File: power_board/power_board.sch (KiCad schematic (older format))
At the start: 84 parts, among them J1 PROG, J10 M4, J11 5V_1, J12 M5, J13 M6, J14 M7, J15 FAN, J16 Screw_Terminal_01x02, J17 MB_interface, J18 Conn_01x02_Female, J19 12V_1, J2 M1, J20 12V_2, J21 12V_3, J22 12V_4, J23 48V_1, J24 48V_2, J25 48V_3, J26 48V_4, J27 Screw_Terminal_01x02, J3 M2, J4 Conn_01x02_Female, J5 Conn_01x02_Female, J6 Conn_01x01_Male, J7 Conn_01x01_Male, J8 Screw_Terminal_01x02, J9 M3, SW1 SW_Push, U1 ACS758xCB-050B-PFF, U10 MAX31855KASA, U2 ACS758xCB-050B-PFF, U3 MCP2515-EST, U4 MAX31855KASA, U5 ATA6560,1, U6 BTS50085-1TMA, U7 ATmega328P-AU, U8 BTS50085-1TMA, U9 LM2596S-5, Y1 20Mhz, Y2 16Mhz

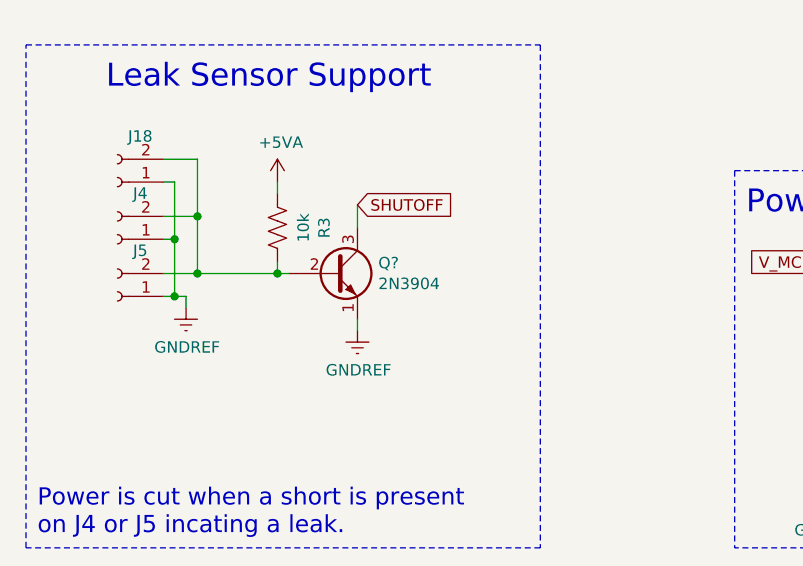
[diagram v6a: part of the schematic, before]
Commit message: selected new footprint for BJT for power shutoff
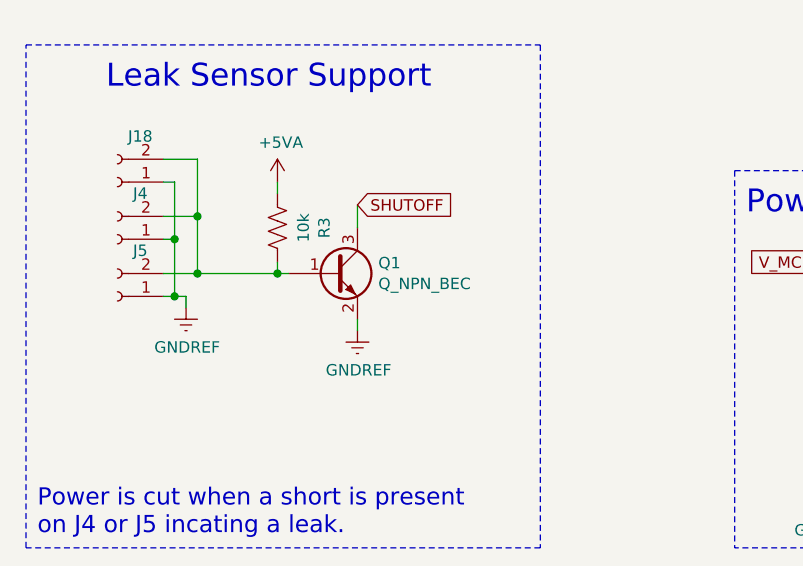
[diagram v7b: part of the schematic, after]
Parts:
- removed Q?: 2N3904, Package_TO_SOT_THT:TO-92_Inline, symbol Transistor_BJT:2N3904
- added Q1: Q_NPN_BEC, Package_TO_SOT_SMD:SOT-23, symbol Device:Q_NPN_BEC
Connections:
- net GNDREF: now also Q1.2 (E)
- net SHUTOFF: now also Q1.3 (C)
- net at J18.2 (Pin_2), J4.2 (Pin_2), J5.2 (Pin_2)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: now also Q1.1 (B)
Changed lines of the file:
@@
-$EndComp
-$Comp
-L power:+5V #PWR0139
-U 1 1 5BB11F6E
-P 6750 3550
-F 0 "#PWR0139" H 6750 3400 50  0001 C CNN
-F 1 "+5V" H 6765 3723 50  0000 C CNN
-F 2 "" H 6750 3550 50  0001 C CNN
-F 3 "" H 6750 3550 50  0001 C CNN
-	1    6750 3550
-	1    0    0    -1
 $EndComp
 $Comp
@@
 	7550 4300 7700 4300
 Connection ~ 7550 4300
-$Comp
-L power:+5V #PWR0142
-U 1 1 5BB53379
-P 7550 3950
-F 0 "#PWR0142" H 7550 3800 50  0001 C CNN
-F 1 "+5V" H 7565 4123 50  0000 C CNN
-F 2 "" H 7550 3950 50  0001 C CNN
-F 3 "" H 7550 3950 50  0001 C CNN
-	1    7550 3950
-	1    0    0    -1
-$EndComp
-Wire Wire Line
-	7550 4000 7550 3950
 $Comp
 L Connector:Screw_Terminal_01x02 J8
@@
 $EndComp
 $Comp
-L power:+5V #PWR0163
-U 1 1 5C02E9E2
-P 6750 5300
-F 0 "#PWR0163" H 6750 5150 50  0001 C CNN
-F 1 "+5V" H 6765 5473 50  0000 C CNN
-F 2 "" H 6750 5300 50  0001 C CNN
-F 3 "" H 6750 5300 50  0001 C CNN
-	1    6750 5300
-	1    0    0    -1
-$EndComp
-$Comp
 L power:GNDREF #PWR0164
 U 1 1 5C02E9E8
@@
 Connection ~ 7550 6050
 $Comp
-L power:+5V #PWR0166
-U 1 1 5C02EA0C
-P 7550 5700
-F 0 "#PWR0166" H 7550 5550 50  0001 C CNN
-F 1 "+5V" H 7565 5873 50  0000 C CNN
-F 2 "" H 7550 5700 50  0001 C CNN
-F 3 "" H 7550 5700 50  0001 C CNN
-	1    7550 5700
-	1    0    0    -1
-$EndComp
-Wire Wire Line
-	7550 5750 7550 5700
-$Comp
 L Connector:Screw_Terminal_01x02 J27
 U 1 1 5C02EA13
@@
 Text Notes 14850 7800 0    75   ~ 0
 ICSP Connections\n
-$Comp
-L Transistor_BJT:2N3904 Q?
-U 1 1 5BF7B85C
+Wire Wire Line
+	2150 8200 2150 8250
+Wire Wire Line
+	2500 8400 2500 8300
+Wire Wire Line
+	2500 8800 2500 8850
+Wire Wire Line
+	1800 8600 2150 8600
+$Comp
+L Device:Q_NPN_BEC Q1
+U 1 1 5C017B6E
 P 2400 8600
-F 0 "Q?" H 2591 8646 50  0000 L CNN
-F 1 "2N3904" H 2591 8555 50  0000 L CNN
-F 2 "Package_TO_SOT_THT:TO-92_Inline" H 2600 8525 50  0001 L CIN
-F 3 "https://www.fairchildsemi.com/datasheets/2N/2N3904.pdf" H 2400 8600 50  0001 L CNN
+F 0 "Q1" H 2591 8646 50  0000 L CNN
+F 1 "Q_NPN_BEC" H 2591 8555 50  0000 L CNN
+F 2 "Package_TO_SOT_SMD:SOT-23" H 2600 8700 50  0001 C CNN
+F 3 "~" H 2400 8600 50  0001 C CNN
 	1    2400 8600
 	1    0    0    -1
 $EndComp
 Wire Wire Line
-	2150 8200 2150 8250
-Wire Wire Line
-	2500 8400 2500 8300
-Wire Wire Line
-	2500 8800 2500 8850
-Wire Wire Line
-	1800 8600 2150 8600
+	7550 5750 7550 5700
+Wire Wire Line
+	7550 4000 7550 3950
+$Comp
+L power:+5V #PWR0142
+U 1 1 5BB53379
+P 7550 3950
+F 0 "#PWR0142" H 7550 3800 50  0001 C CNN
+F 1 "+5V" H 7565 4123 50  0000 C CNN
+F 2 "" H 7550 3950 50  0001 C CNN
+F 3 "" H 7550 3950 50  0001 C CNN
+	1    7550 3950
+	1    0    0    -1
+$EndComp
+$Comp
+L power:+5V #PWR0166
+U 1 1 5C02EA0C
+P 7550 5700
+F 0 "#PWR0166" H 7550 5550 50  0001 C CNN
+F 1 "+5V" H 7565 5873 50  0000 C CNN
+F 2 "" H 7550 5700 50  0001 C CNN
+F 3 "" H 7550 5700 50  0001 C CNN
+	1    7550 5700
+	1    0    0    -1
+$EndComp
+$Comp
+L power:+5V #PWR0163
+U 1 1 5C02E9E2
+P 6750 5300
+F 0 "#PWR0163" H 6750 5150 50  0001 C CNN
+F 1 "+5V" H 6765 5473 50  0000 C CNN
+F 2 "" H 6750 5300 50  0001 C CNN
+F 3 "" H 6750 5300 50  0001 C CNN
+	1    6750 5300
+	1    0    0    -1
+$EndComp
+$Comp
+L power:+5V #PWR0139
+U 1 1 5BB11F6E
+P 6750 3550
+F 0 "#PWR0139" H 6750 3400 50  0001 C CNN
+F 1 "+5V" H 6765 3723 50  0000 C CNN
+F 2 "" H 6750 3550 50  0001 C CNN
+F 3 "" H 6750 3550 50  0001 C CNN
+	1    6750 3550
+	1    0    0    -1
+$EndComp
 $EndSCHEMATC

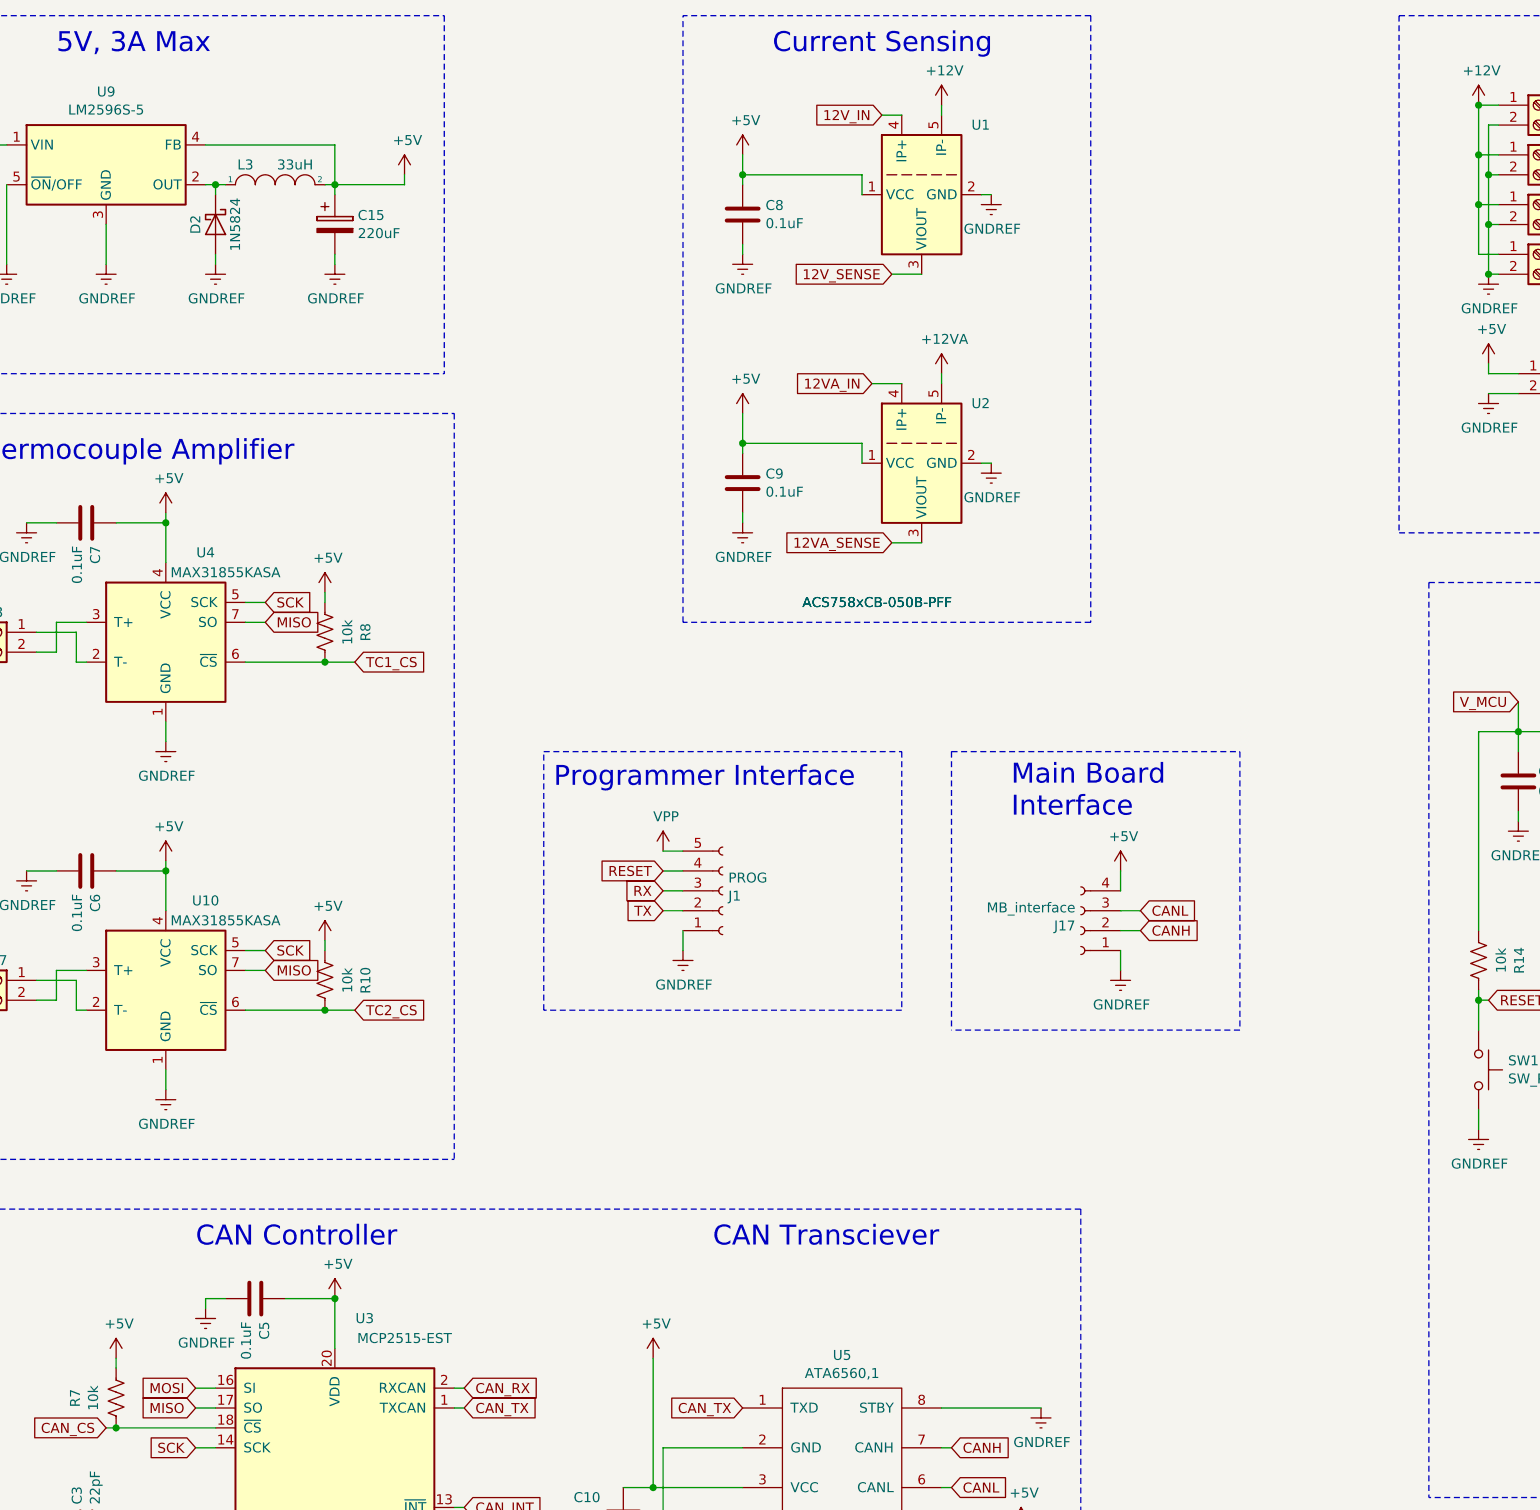
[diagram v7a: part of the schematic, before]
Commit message: Adding 3.3v regulator hardware for TC amps
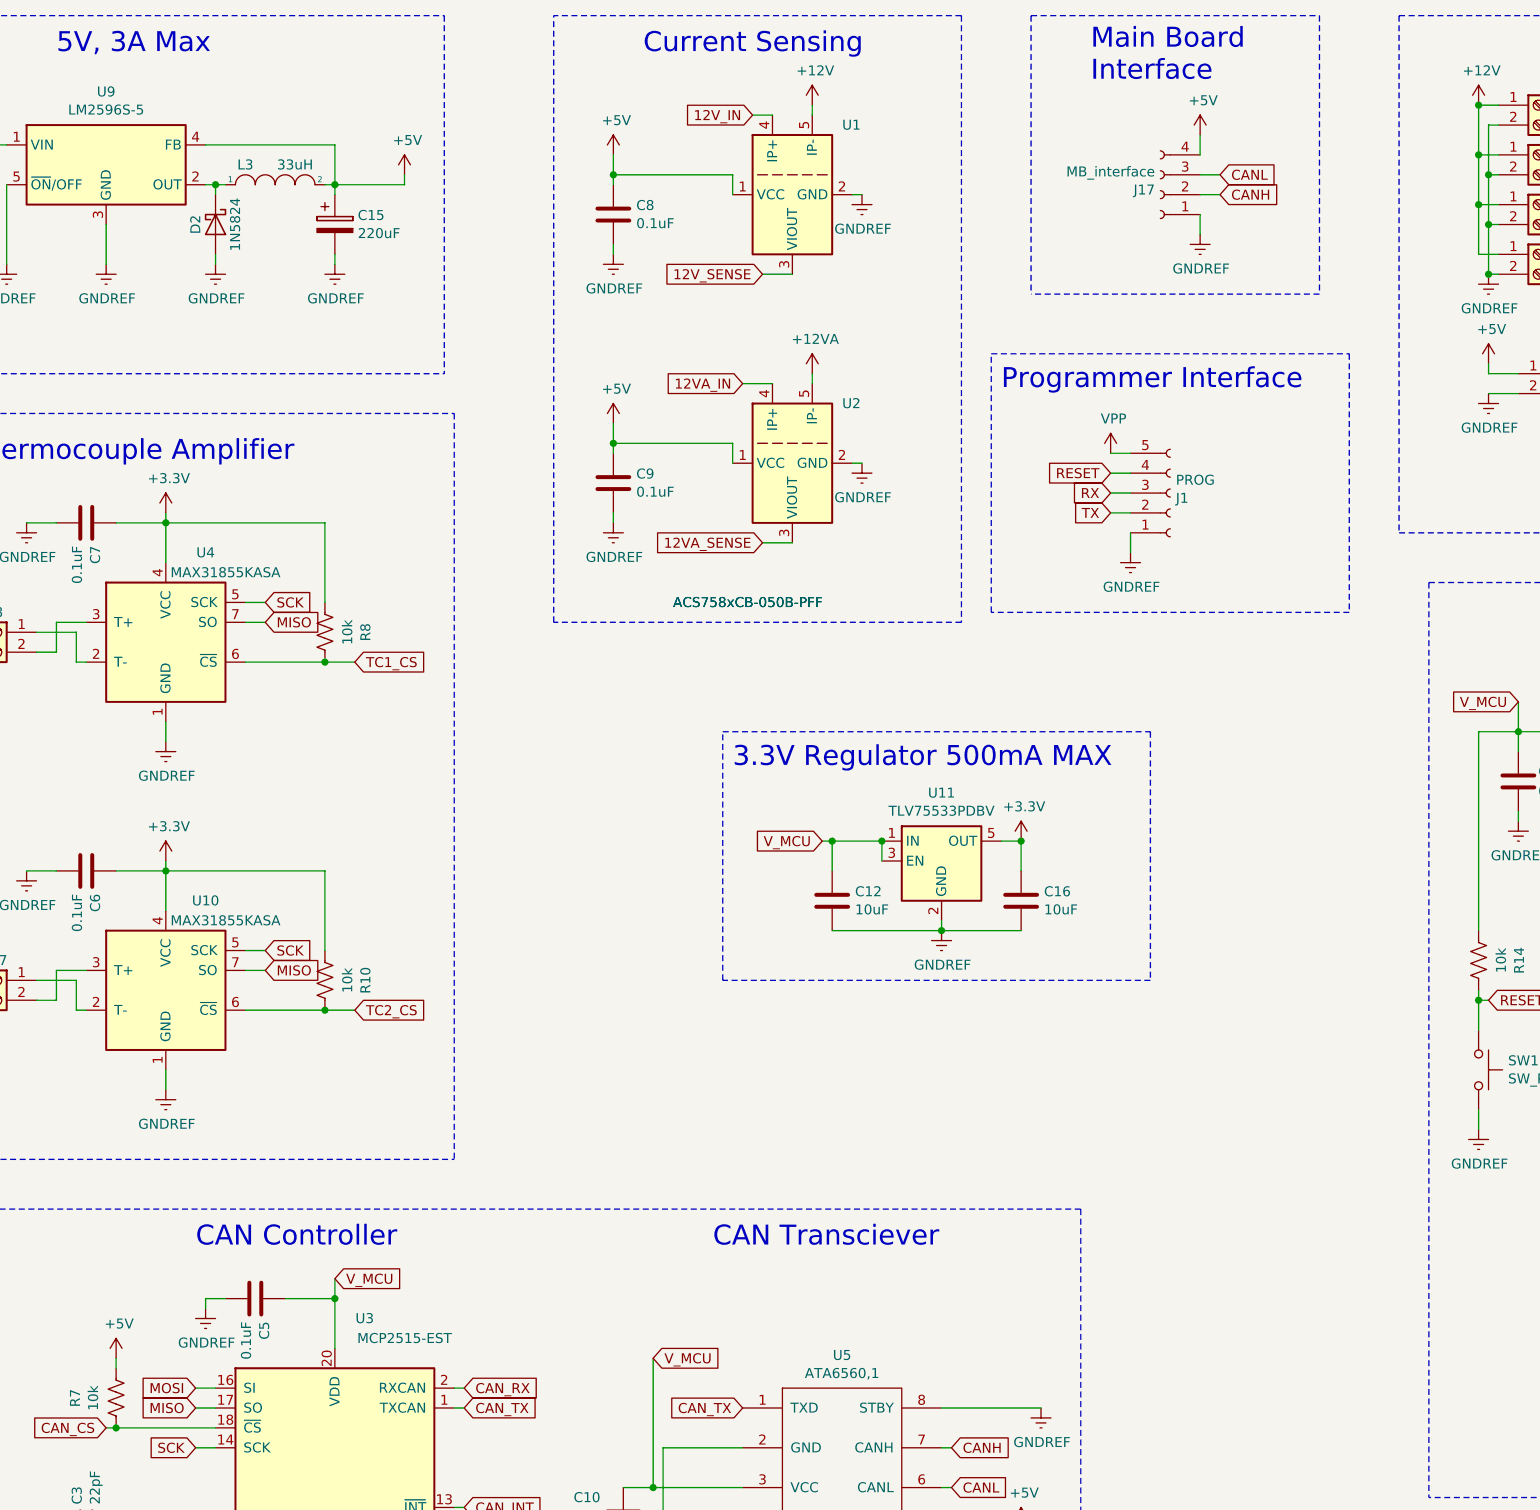
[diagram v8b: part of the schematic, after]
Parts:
- added C12, C16: 10uF, Capacitor_SMD:C_0805_2012Metric, symbol Device:C
- added U11: TLV75533PDBV, Package_TO_SOT_SMD:SOT-23-5, symbol Regulator_Linear:TLV75533PDBV
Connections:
- net +5V: no longer C10.1, C5.1, C6.1, C7.1, R10.1, R8.1, U10.4 (VCC), U3.20 (VDD), U4.4 (VCC), U5.3 (VCC)
- net GNDREF: now also C12.2, C16.2, U11.2 (GND)
- net V_MCU: now also C10.1, C5.1, U3.20 (VDD), U5.3 (VCC), C12.1, U11.1 (IN), U11.3 (EN)
- new net +3V3: C16.1, C6.1, C7.1, R10.1, R8.1, U10.4 (VCC), U11.5 (OUT), U4.4 (VCC)
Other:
- note added: "3.3V Regulator 500mA MAX\n\n"
- moved on the sheet: C8, C9, J1, J17, U1, U2
